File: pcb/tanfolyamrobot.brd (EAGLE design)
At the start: 81.3 x 58.7 mm, 78 parts, among them IC1 STM32F10XRXT6, IC2 7805, IC4 FT232RL, IC5 LD117AS33TR, M1 DRV8833, Q2 BSS123, Q3 BSS123, Q4 BSS123, X1 CSTCE08M, X2 PWR, X6 KUSBVX-BS1N

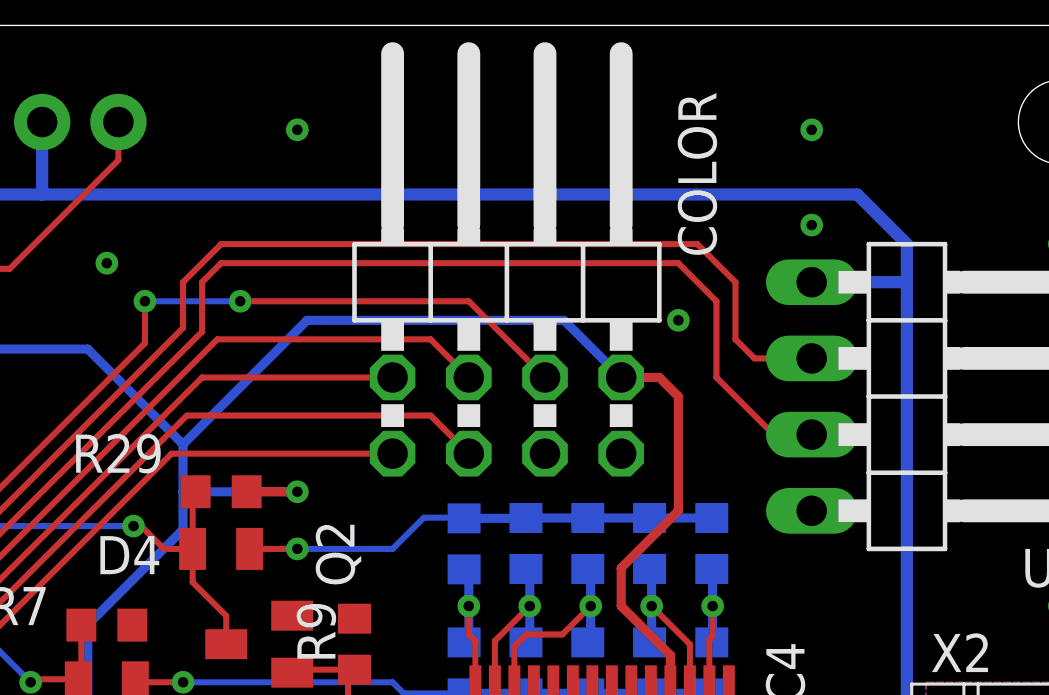
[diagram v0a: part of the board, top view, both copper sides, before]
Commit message: added 5V pull-up for ultrasonic trigger (#1)
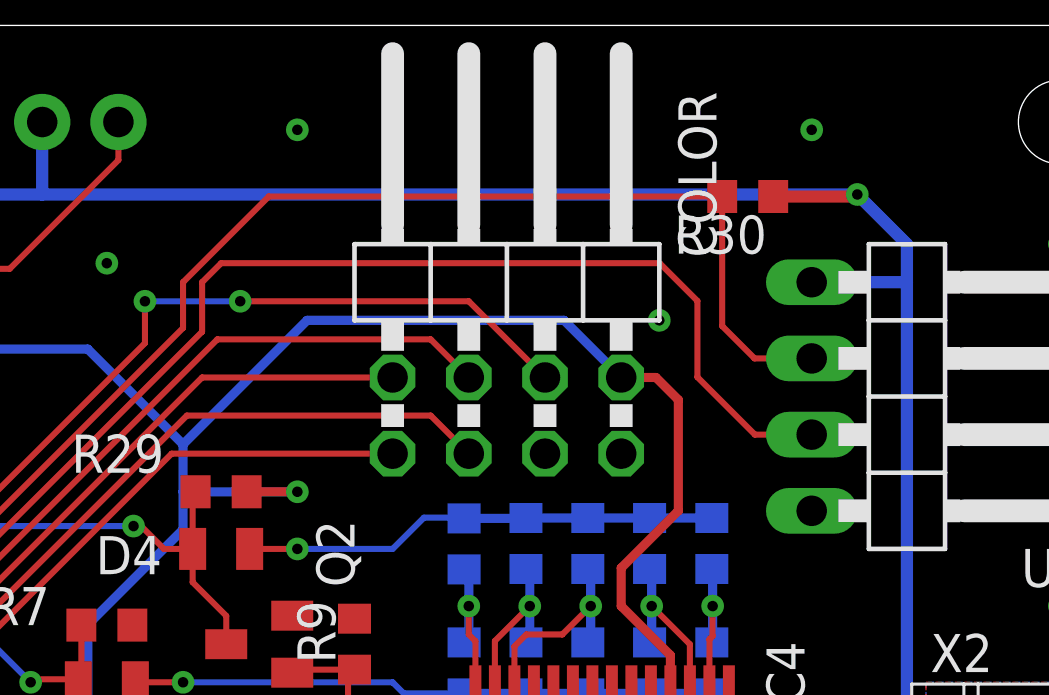
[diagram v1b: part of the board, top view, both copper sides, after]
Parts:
- added R30: 4K7, rcl:R0603
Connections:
- net +5V: now also R30.1
- net US_TRIG: now also R30.2
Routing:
- net +5V: track 209.3 -> 212.1 mm, vias 3 -> 4
- net US_TRIG: track 43.4 -> 46.1 mm
- net GND: vias 55 -> 54
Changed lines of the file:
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@@
 <grid distance="25" unitdist="mil" unit="mil" style="dots" multiple="1" display="yes" altdistance="6.125" altunitdist="mil" altunit="mil"/>
 <layers>
-<layer number="1" name="Top" color="4" fill="1" visible="yes" active="yes"/>
+<layer number="1" name="Top" color="4" fill="1" visible="no" active="yes"/>
 <layer number="2" name="Route2" color="16" fill="1" visible="no" active="no"/>
 <layer number="3" name="Route3" color="17" fill="1" visible="no" active="no"/>
@@
 <layer number="19" name="Unrouted" color="6" fill="1" visible="yes" active="yes"/>
 <layer number="20" name="Dimension" color="24" fill="1" visible="yes" active="yes"/>
-<layer number="21" name="tPlace" color="7" fill="1" visible="yes" active="yes"/>
+<layer number="21" name="tPlace" color="7" fill="1" visible="no" active="yes"/>
 <layer number="22" name="bPlace" color="7" fill="1" visible="yes" active="yes"/>
-<layer number="23" name="tOrigins" color="13" fill="1" visible="yes" active="yes"/>
+<layer number="23" name="tOrigins" color="13" fill="1" visible="no" active="yes"/>
 <layer number="24" name="bOrigins" color="13" fill="1" visible="yes" active="yes"/>
 <layer number="25" name="tNames" color="7" fill="1" visible="no" active="yes"/>
@@
 <layer number="37" name="tTest" color="7" fill="1" visible="no" active="yes"/>
 <layer number="38" name="bTest" color="7" fill="1" visible="no" active="yes"/>
-<layer number="39" name="tKeepout" color="4" fill="11" visible="yes" active="yes"/>
+<layer number="39" name="tKeepout" color="4" fill="11" visible="no" active="yes"/>
 <layer number="40" name="bKeepout" color="1" fill="11" visible="yes" active="yes"/>
-<layer number="41" name="tRestrict" color="4" fill="10" visible="yes" active="yes"/>
+<layer number="41" name="tRestrict" color="4" fill="10" visible="no" active="yes"/>
 <layer number="42" name="bRestrict" color="1" fill="10" visible="yes" active="yes"/>
 <layer number="43" name="vRestrict" color="2" fill="10" visible="no" active="yes"/>
@@
 <layer number="49" name="Reference" color="7" fill="1" visible="no" active="yes"/>
 <layer number="50" name="dxf" color="7" fill="1" visible="no" active="no"/>
-<layer number="51" name="tDocu" color="7" fill="1" visible="yes" active="yes"/>
+<layer number="51" name="tDocu" color="7" fill="1" visible="no" active="yes"/>
 <layer number="52" name="bDocu" color="7" fill="1" visible="yes" active="yes"/>
 <layer number="53" name="tGND_GNDA" color="7" fill="9" visible="no" active="no"/>
@@
 <attribute name="VBR" value="6V" x="64.77" y="18.415" size="1.778" layer="27" rot="R90" display="off"/>
 </element>
+<element name="R30" library="rcl" library_urn="urn:adsk.eagle:library:334" package="R0603" package3d_urn="urn:adsk.eagle:package:23555/3" value="4K7" x="67.7164" y="53.0225" smashed="yes" rot="R180">
+<attribute name="NAME" x="68.3514" y="52.3875" size="1.27" layer="25" rot="R180"/>
+<attribute name="POPULARITY" value="70" x="67.7164" y="53.0225" size="1.778" layer="27" rot="R180" display="off"/>
+<attribute name="SPICEPREFIX" value="R" x="67.7164" y="53.0225" size="1.778" layer="27" rot="R180" display="off"/>
+<attribute name="VALUE" x="68.3514" y="54.9275" size="1.27" layer="27" rot="R180"/>
+</element>
 </elements>
 <signals>
@@
 <via x="4.445" y="19.05" extent="1-16" drill="0.35"/>
 <via x="53.34" y="26.67" extent="1-16" drill="0.7" diameter="1.524"/>
-<via x="65.405" y="48.895" extent="1-16" drill="0.35"/>
+<via x="64.77" y="48.895" extent="1-16" drill="0.35"/>
 <via x="46.355" y="50.8" extent="1-16" drill="0.35"/>
-<via x="69.85" y="52.07" extent="1-16" drill="0.35"/>
 <contactref element="IC5" pad="1"/>
 <via x="61.595" y="6.985" extent="1-16" drill="0.35"/>
@@
 <wire x1="45.72" y1="32.385" x2="44.45" y2="31.115" width="0.3048" layer="16"/>
 <wire x1="65.14" y1="36.645" x2="65.14" y2="37.73" width="0.3048" layer="1"/>
-<wire x1="65.405" y1="46.355" x2="64.77" y2="46.99" width="0.3048" layer="1"/>
-<wire x1="64.77" y1="46.99" x2="63.5" y2="46.99" width="0.3048" layer="1"/>
+<wire x1="65.405" y1="46.243875" x2="64.658875" y2="46.99" width="0.3048" layer="1"/>
+<wire x1="64.658875" y1="46.99" x2="63.5" y2="46.99" width="0.3048" layer="1"/>
 <wire x1="65.14" y1="37.73" x2="63.5" y2="39.37" width="0.3048" layer="1"/>
 <wire x1="63.5" y1="39.37" x2="63.5" y2="40.64" width="0.3048" layer="1"/>
 <wire x1="63.5" y1="40.64" x2="65.405" y2="42.545" width="0.3048" layer="1"/>
-<wire x1="65.405" y1="42.545" x2="65.405" y2="46.355" width="0.3048" layer="1"/>
+<wire x1="65.405" y1="42.545" x2="65.405" y2="46.243875" width="0.3048" layer="1"/>
 <wire x1="45.07" y1="5.095" x2="45.1625" y2="5.095" width="0.3048" layer="16"/>
 <wire x1="40.005" y1="6.35" x2="43.815" y2="6.35" width="0.3048" layer="16"/>
@@
 <wire x1="73.025" y1="32.385" x2="69.43" y2="32.385" width="0.4064" layer="1"/>
 <wire x1="69.43" y1="32.385" x2="69.342" y2="32.297" width="0.4064" layer="1"/>
+<contactref element="R30" pad="1"/>
+<wire x1="68.5664" y1="53.0225" x2="71.3025" y2="53.0225" width="0.4064" layer="1"/>
+<wire x1="71.3025" y1="53.0225" x2="71.37" y2="53.09" width="0.2032" layer="1"/>
+<via x="71.37" y="53.09" extent="1-16" drill="0.35"/>
 </signal>
 <signal name="FTDI_RSTN">
@@
 <wire x1="35.531625" y1="38.197415625" x2="37.974209375" y2="40.64" width="0.2032" layer="1"/>
 <wire x1="40.894" y1="40.64" x2="48.895" y2="48.641" width="0.2032" layer="1"/>
-<wire x1="48.895" y1="48.641" x2="48.895" y2="50.165" width="0.2032" layer="1"/>
-<wire x1="48.895" y1="50.165" x2="50.165" y2="51.435" width="0.2032" layer="1"/>
+<wire x1="48.895" y1="50.165" x2="48.895" y2="48.641" width="0.2032" layer="1"/>
 <wire x1="37.974209375" y1="40.64" x2="40.894" y2="40.64" width="0.2032" layer="1"/>
-<wire x1="66.04" y1="51.435" x2="67.31" y2="50.165" width="0.2032" layer="1"/>
-<wire x1="67.31" y1="48.26" x2="67.945" y2="47.625" width="0.2032" layer="1"/>
-<wire x1="67.945" y1="47.625" x2="69.85" y2="47.625" width="0.2032" layer="1"/>
-<wire x1="50.165" y1="51.435" x2="66.04" y2="51.435" width="0.2032" layer="1"/>
-<wire x1="67.31" y1="50.165" x2="67.31" y2="48.26" width="0.2032" layer="1"/>
+<contactref element="R30" pad="2"/>
+<wire x1="69.85" y1="47.625" x2="67.945" y2="47.625" width="0.2032" layer="1"/>
+<wire x1="66.8664" y1="48.7036" x2="66.8664" y2="53.0225" width="0.2032" layer="1"/>
+<wire x1="67.945" y1="47.625" x2="66.8664" y2="48.7036" width="0.2032" layer="1"/>
+<wire x1="66.8664" y1="53.0225" x2="51.7525" y2="53.0225" width="0.2032" layer="1"/>
+<wire x1="51.7525" y1="53.0225" x2="48.895" y2="50.165" width="0.2032" layer="1"/>
 </signal>
 <signal name="US_ECHO">
 <contactref element="US" pad="3"/>
-<wire x1="68.58" y1="45.085" x2="69.85" y2="45.085" width="0.2032" layer="1"/>
+<wire x1="67.9577" y1="45.085" x2="69.85" y2="45.085" width="0.2032" layer="1"/>
 <contactref element="IC1" pad="58"/>
 <wire x1="35.885178125" y1="37.8438625" x2="38.173315625" y2="40.132" width="0.2032" layer="1"/>
@@
 <wire x1="38.173315625" y1="40.132" x2="41.148" y2="40.132" width="0.2032" layer="1"/>
 <wire x1="41.148" y1="40.132" x2="49.53" y2="48.514" width="0.2032" layer="1"/>
-<wire x1="65.405" y1="50.8" x2="66.675" y2="49.53" width="0.2032" layer="1"/>
-<wire x1="50.165" y1="50.8" x2="65.405" y2="50.8" width="0.2032" layer="1"/>
-<wire x1="66.675" y1="49.53" x2="66.675" y2="46.99" width="0.2032" layer="1"/>
-<wire x1="66.675" y1="46.99" x2="68.58" y2="45.085" width="0.2032" layer="1"/>
+<wire x1="64.7827" y1="50.8" x2="66.04" y2="49.5427" width="0.2032" layer="1"/>
+<wire x1="50.165" y1="50.8" x2="64.7827" y2="50.8" width="0.2032" layer="1"/>
+<wire x1="66.04" y1="49.5427" x2="66.04" y2="47.0027" width="0.2032" layer="1"/>
+<wire x1="66.04" y1="47.0027" x2="67.9577" y2="45.085" width="0.2032" layer="1"/>
 </signal>
 <signal name="ENC1_A_5V">

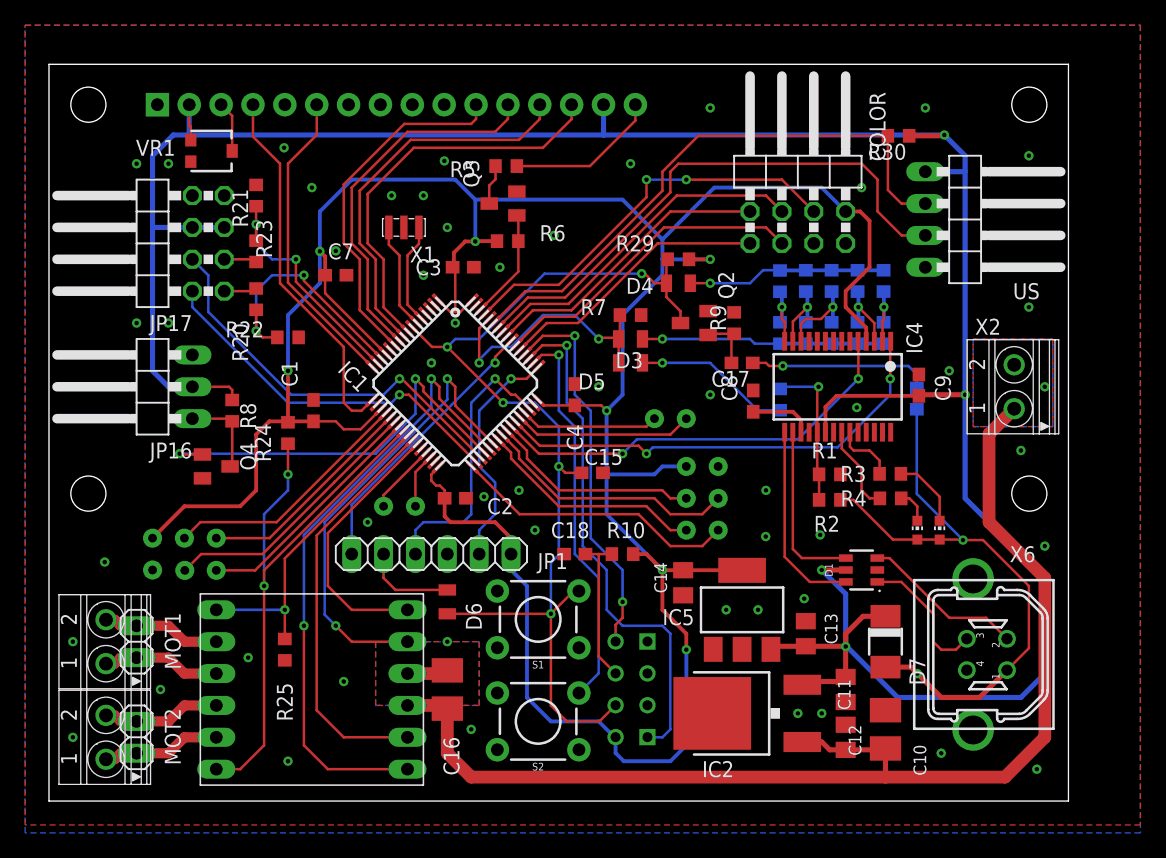
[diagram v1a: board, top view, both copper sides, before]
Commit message: made lots of pcb traces nicer (#1)
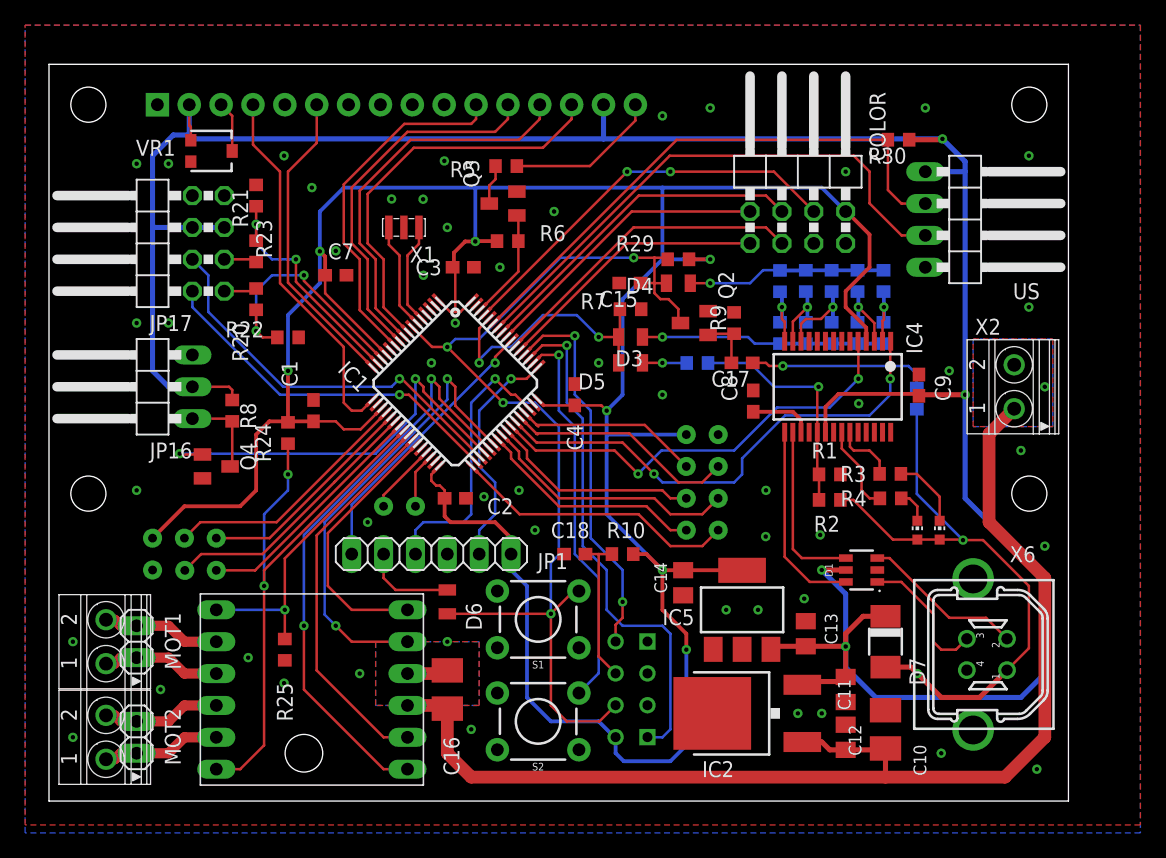
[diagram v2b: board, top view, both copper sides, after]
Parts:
- moved C15 15.4 mm to (46.3, 41.3), turned to 180 degrees
- moved R28 7.21 mm to (51.7, 34.9), turned to 0 degrees
- moved R7 0.47 mm to (46.4, 39.2)
- moved R30 0.31 mm to (67.7, 52.7)
- moved D3 0.16 mm to (46.4, 37.0)
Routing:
- net N$8: track 12.5 -> 3.53 mm
- net FTDI_RSTN: track 12.3 -> 18.7 mm
- net PA11: track 14.2 -> 18.5 mm
- net PA12: track 10.9 -> 14.7 mm
- net USART1_RX: track 37.0 -> 39.6 mm
- net MOTOR1_IN1: track 50.0 -> 47.4 mm
- net MOTOR1_IN2: track 32.7 -> 30.9 mm
- net RSTN: track 82.8 -> 84.2 mm, vias 5 -> 4
- net USART1_TX: track 33.9 -> 35.2 mm
- net US_TRIG: track 46.1 -> 44.8 mm
- net +5V: track 212.1 -> 213.3 mm
- net ENC2_B_5V: track 32.4 -> 31.9 mm
- net ENC2_A_5V: track 29.6 -> 29.1 mm
